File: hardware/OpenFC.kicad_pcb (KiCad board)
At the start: 8 copper layers, 37.5 x 37.5 mm, 226 parts, among them J1 5V, J10 5V, J11 5V, J12 5V, J16 5V, J17 5V, J18 5V, J19 5V, J2 5V, J20 5V, J21 5V, J22 5V, J23 5V, J24 5V, J25 5V, J26 5V, J27 5V, J28 5V, J29 5V, J3 5V, J30 5V, J31 5V, J32 5V, J33 5V, J34 5V, J35 5V, J36 5V, J38 5V, J39 5V, J4 5V, J40 5V, J43 5V, J44 5V, J45 5V, J46 5V, J49 5V, J5 5V, J50 5V, J51 5V, J52 5V, J53 5V, J54 5V, J55 5V, J56 5V, J57 5V, J58 5V, J59 5V, J6 5V, J7 5V, J8 5V, J9 5V, P1 SM08B-SRSS-TB(LF)(SN), Q1 DMN1150UFB-7B, Q2 DMN1150UFB-7B, Q7 DMN1150UFB-7B, U1 SM06B-SRSS-TB(LF)(SN), U10 TXU0101DRYR, U12 WL9005D4-33, U13 LP5912-3.3DRVR, U14 LSM6DSV16XTR, U15 XL-1010RGBC-WS2812B, U16 XL-1010RGBC-WS2812B, U17 XL-1010RGBC-WS2812B, U18 XL-1010RGBC-WS2812B, U19 XL-1010RGBC-WS2812B, U2 ESP32-C3FH4, U20 SX1281IMLTRT, U21 NCV8187AMT180TAG, U22 XL-1010RGBC-WS2812B, U23 XL-1010RGBC-WS2812B, U24 XL-1010RGBC-WS2812B, U25 XL-1010RGBC-WS2812B, U26 XL-1010RGBC-WS2812B, U27 XL-1010RGBC-WS2812B, U28 XL-1010RGBC-WS2812B, U29 XL-1010RGBC-WS2812B, U3 XL-1010RGBC-WS2812B, U30 BMP388, U32 TS2306A 240GF MSM 9_C2976675, U33 TPS2116DRLR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

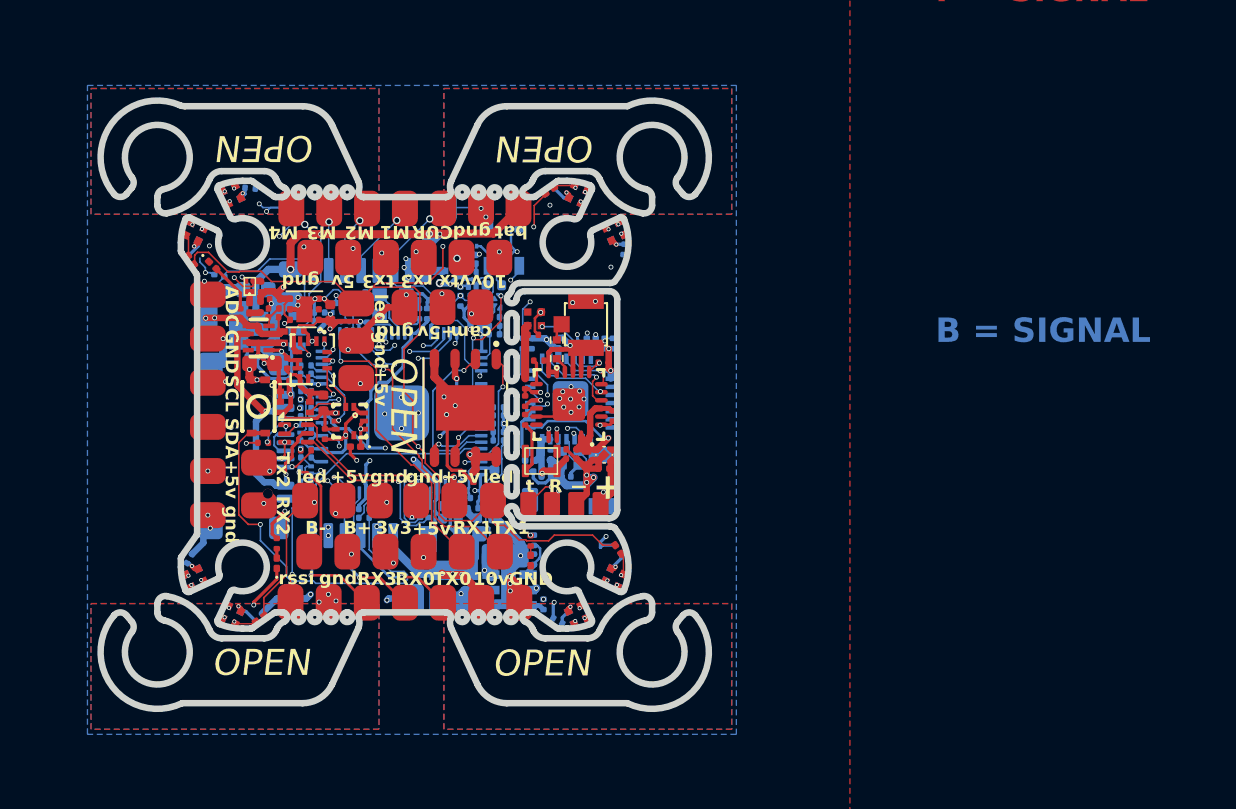
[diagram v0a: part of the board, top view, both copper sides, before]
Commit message: Standardize repo: .gitignore, README, license, remove orphaned files
- Standardize .gitignore to match ecosystem template
- Fix README: correct GitHub URL, remove generic sections, remove nonexistent dirs
- Replace LICENSE stub with full CERN-OHL-S-2.0 text
- Remove orphaned schematics (baro, blackbox, compass, elrs, leds) — not in ECO variant
- Delete self-referential symlink and parent OpenFC production leftovers
- Add new footprints and 3D models (SIM, TF connectors)

Co-Authored-By: Claude Opus 4.6 (1M context) <noreply@anthropic.com>
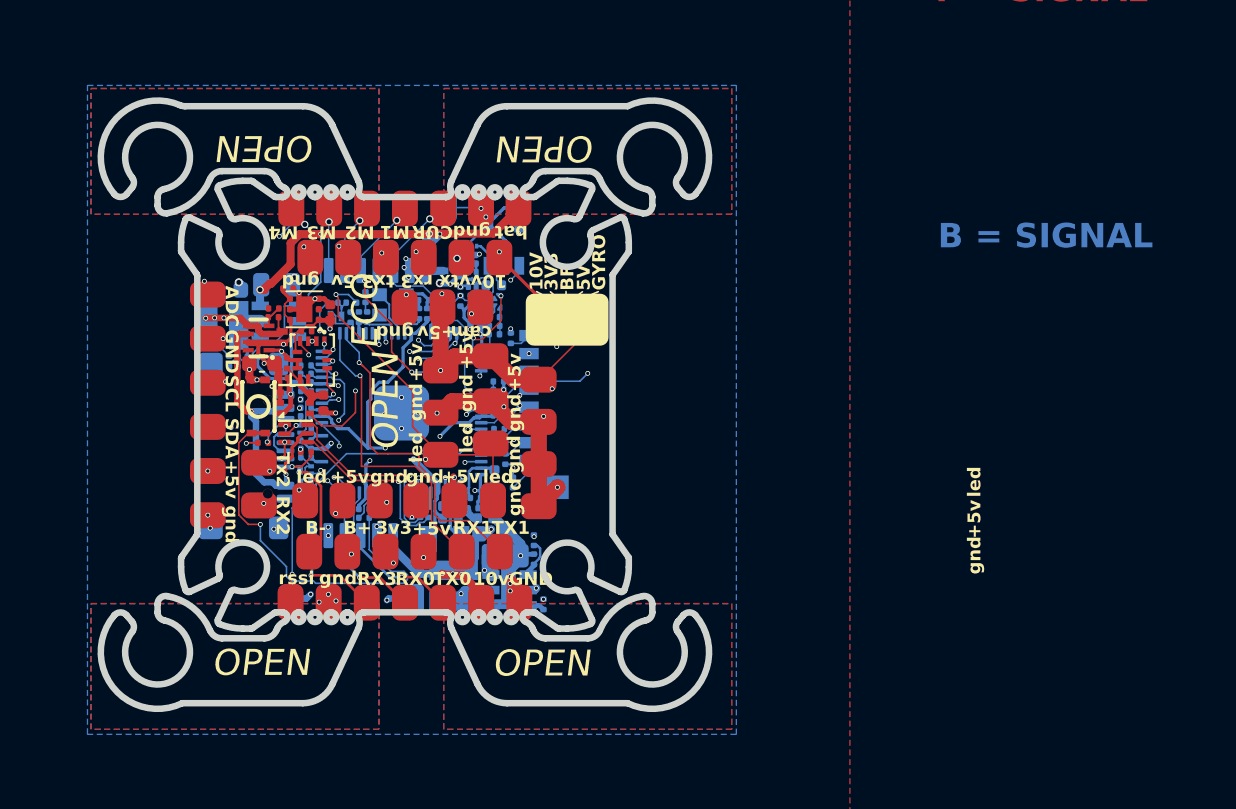
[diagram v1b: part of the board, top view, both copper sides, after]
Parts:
- removed AE1: 2450AT18A100E, lib:ANT-SMD_L3.2-W1.6
- removed C11, C12, C13, C14, C18, C19, C20, C21, C22, C23, C24, C25, C26, C45, C46, C47, C5, C53, C54, C55, C57, C58, C63, C8: 100n, Capacitor_SMD:C_0201_0603Metric
- removed C15: 1n, Capacitor_SMD:C_0201_0603Metric
- removed C17: 22uF, Capacitor_SMD:C_0402_1005Metric
- removed C4, C6: 12p, Capacitor_SMD:C_0201_0603Metric
- removed C7: 470nF, Capacitor_SMD:C_0201_0603Metric
- removed C9: 10nF, Capacitor_SMD:C_0201_0603Metric
- removed FL1: DEA102700LT-6307A2, lib:FILTER-SMD_4P-L1.0-W0.5-L
- removed J10, J11, J12, J26, J31: 5V, lib:small_pad
- removed JP1, JP2, JP3, JP4: SolderJumper_2_Open, Panelization:MouseBite-Slot-Jumper_0201
- removed L7: LQG15HS2N0S02D, lib:L0402
- removed OSC1: OW7EL89CENUNFAYLC-52M, lib:OSC-SMD_4P-L2.0-W1.6-BL_TXC_7Z
- removed R26: 1k, Capacitor_SMD:C_0201_0603Metric
- removed RF1: CONUFL001-SMD-T, lib:IPEX-SMD_3P-L2.6-W2.6-LS3.0
- removed U10: TXU0101DRYR, lib:SON-6_L1.5-W1.0-P0.50-TL
- removed U12: WL9005D4-33, lib:UDFN-4_L1.0-W1.0-P0.65-TL
- removed U15, U16, U17, U18, U19, U22, U23, U24, U25, U26, U27, U28, U29, U3, U4, U5, U8: XL-1010RGBC-WS2812B, lib:LED-SMD_4P-L1.0-W1.0-TL_XL-1010RGBC-WS2812B
- removed U2: ESP32-C3FH4, lib:QFN-32_L5.0-W5.0-P0.50-TL-EP3.7
- removed U20: SX1281IMLTRT, lib:QFN-24_L4.0-W4.0-P0.50-TL-EP2.6
- removed U30: BMP388, lib:SENSORM-SMD_BMP388
- removed U9: W25Q128JVPIQ, lib:WSON-8_L6.0-W5.0-P1.27-BL-EP
- removed X2: SX0B40.000F0810F30, lib:CRYSTAL-SMD_4P-L1.6-W1.2-BL
- added C1: 100n, Capacitor_SMD:C_0201_0603Metric, B.Cu at (158.4, 88.0)
- added Card2: TF-021B-H265, lib:TF-SMD_TF-021B-H265, B.Cu at (161.5, 86.2)
- added J13: 5V, lib:small_pad, F.Cu at (157.9, 83.5)
- added J14: 5V, lib:small_pad, F.Cu at (157.9, 86.3)
- added J15: 5V, lib:small_pad, F.Cu at (157.9, 88.9)
- added J41: 5V, lib:small_pad, F.Cu at (160.8, 92.8)
- added J42: 5V, lib:small_pad, F.Cu at (160.8, 90.2)
- added J47: 5V, lib:small_pad, F.Cu at (160.8, 87.5)
- added J48: 5V, lib:small_pad, F.Cu at (160.8, 85.0)
- added Q3: DMN1150UFB-7B, lib:DFN-3L_L1.0-W0.6-P0.65-BR, B.Cu at (148.3, 81.0)
- R2: moved to B.Cu
- R6: value 10k -> 2.2k; moved to B.Cu
- R9: value 1k -> 2.2k
- moved D4 23.2 mm to (162.0, 80.8), turned to -90 degrees
- moved D1 22.5 mm to (163.0, 80.8), turned to -90 degrees
- moved R4 21.7 mm to (162.0, 82.0), turned to 90 degrees
- moved Q1 21.3 mm to (164.3, 80.6), turned to -90 degrees
- moved R15 20.6 mm to (163.0, 81.9)
- moved R19 20.6 mm to (164.2, 81.9)
- moved D7 20.6 mm to (163.6, 80.8)
- moved R12 20.0 mm to (163.6, 81.9), turned to 90 degrees
- moved R9 15.9 mm to (148.2, 80.2), turned to 0 degrees
- moved D2 15.4 mm to (162.5, 80.8), turned to -90 degrees
- moved D5 15.4 mm to (161.5, 80.8), turned to -90 degrees
- moved R29 13.0 mm to (161.5, 82.0), turned to 90 degrees
- moved R6 11.9 mm to (149.2, 81.1)
- moved J18 10.7 mm to (154.8, 89.6), turned to 0 degrees
- moved R1 9.97 mm to (159.3, 91.3), turned to 90 degrees
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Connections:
- J27 pad 1: unconnected-(J27-Pin_1-Pad1) -> +BATT
- R1 pad 1: +3.3V_ELRS -> Net-(Card2-DAT2)
- R1 pad 2: Net-(J12-Pin_1) -> +3.3V
- R2 pad 1: +3.3V_ELRS -> /BLACKBOX/BB_CS
- R2 pad 2: /ELRS/CS -> +3.3V
- R3 pad 1: +3.3V_ELRS -> Net-(Card2-DAT1)
- R3 pad 2: Net-(U2-CHIP_EN) -> +3.3V
- R34 pad 1: Net-(U10-BY) -> Net-(Q3-D)
- R6 pad 1: +3.3V_ELRS -> +3.3V
- R6 pad 2: /ELRS/RST -> /RP2350A/LED_STRIP_L
- R9 pad 1: /ELRS/ESP_BOOT0 -> +5V
- R9 pad 2: Net-(J12-Pin_1) -> Net-(Q3-D)
- U14 pad 9: unconnected-(U14-INT2-Pad9) -> /IMU/SPI0.CLKIN
- U36 pad 25: /ELRS/ESP8285_EN -> /RP2350A/ESP_EN
- U36 pad 26: /ELRS/ESP_BOOT0 -> /RP2350A/ESP_BOOT
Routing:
- net GND: track 163.5 -> 93.1 mm, vias 93 -> 56
- net /LED: track 83.1 -> 31.0 mm, vias 5 -> 3
- net +5V_BUCK: track 10.0 -> 39.6 mm, vias 2 -> 4
- net +3.3V: track 52.7 -> 78.4 mm, vias 17 -> 18
- net +3.3V_ELRS: track 22.2 -> 0.00 mm, vias 7 -> 0
- net /UART1_RX: track 40.6 -> 18.7 mm, vias 3 -> 1
- net /UART1_TX: track 41.3 -> 19.8 mm, vias 3 -> 1
- net /ELRS/ESP_BOOT0: track 20.8 -> 0.00 mm, vias 2 -> 0
- net /ELRS/ESP8285_EN: track 18.8 -> 0.00 mm, vias 2 -> 0
- net Net-(J12-Pin_1): track 15.5 -> 0.00 mm, vias 2 -> 0
- net +5V: track 49.0 -> 34.7 mm, vias 23 -> 12
- net Net-(D2-A): track 6.22 -> 19.3 mm
- net Net-(U15-DIN): track 12.6 -> 0.00 mm, vias 2 -> 0
- net Net-(U24-DIN): track 12.2 -> 0.00 mm, vias 2 -> 0
- net Net-(U26-DOUT): track 12.0 -> 0.00 mm, vias 2 -> 0
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- added copper zone on In2.Cu, net +3.3V
- added copper zone on In4.Cu, net GND
- removed copper zone on In4.Cu, net +3.3V
- removed copper zone on In4.Cu, net +3.3V_ELRS
- removed copper zone on In5.Cu, net GND
- removed copper zone on In6.Cu, net GND
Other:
- outline, holes or cut-outs redrawn
- copper layers 8 -> 6
- board text added: "10V"
- board text added: "3V3"
- board text added: "5V"
- board text added: "BF"
- board text added: "ECO"
- board text added: "GYRO"
- board text added: "LN4 = Ground"
- board text removed: "+"
- board text removed: "-"
- board text removed: "ELRS"
- board text removed: "LN4 = Signal"
- board text removed: "LN5 = Y-SIGNALS"
- board text removed: "LN6 = GROUND (B Reference)"
- board text removed: "R"
- board text removed: "boot"
- board text removed: "t"

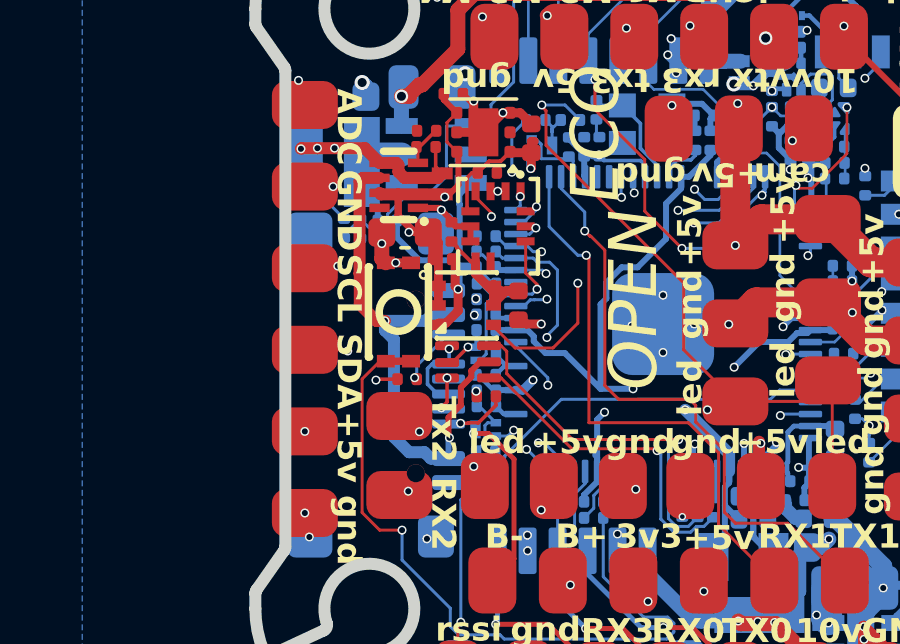
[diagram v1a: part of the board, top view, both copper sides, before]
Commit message: WIP: add blackbox SD card sub-sheet, pre-reroute checkpoint
- Add blackbox.kicad_sch (rebuilt via rebuild_blackbox.py with kicad-sch-api)
  for TF-021B-H265 SD card slot, replacing onboard SPI flash
- Add hardware/tools/rebuild_blackbox.py helper
- Update TF-SMD_TF-021B-H265 footprint
- Save current PCB state before rerouting for DFM and IMU family compatibility

Co-Authored-By: Claude Opus 4.6 (1M context) <noreply@anthropic.com>
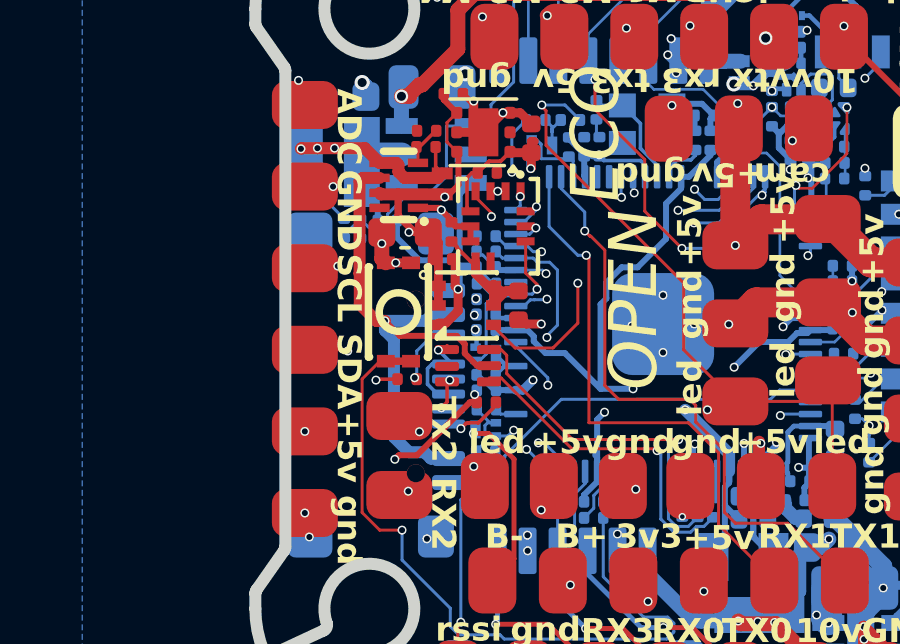
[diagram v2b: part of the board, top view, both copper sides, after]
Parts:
- moved R40 0.20 mm to (146.5, 89.6)
- moved D8 0.13 mm to (145.9, 88.4)
- moved R13 0.11 mm to (146.5, 89.8)
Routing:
- net GND: track 93.1 -> 95.7 mm, vias 56 -> 57
- net +5V_USB: track 18.2 -> 18.5 mm, vias 2 -> 1
